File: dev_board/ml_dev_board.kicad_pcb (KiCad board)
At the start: 2 copper layers, 100 x 73.2 mm, 49 parts, among them J1 JTAG 3.3V, J2 Canon-Service-Connector, J3 USB_B_Mini, J4 Probe Connector, J5 canon_service_jumper_terminal, U1 SN74AUP1T34DCK, U2 SN74AUP1T34DCK, U3 93LCxxBxxOT, U4 LD1117S33TR_SOT223, U5 FT4232H, U6 74HC595, Y1 12MHz

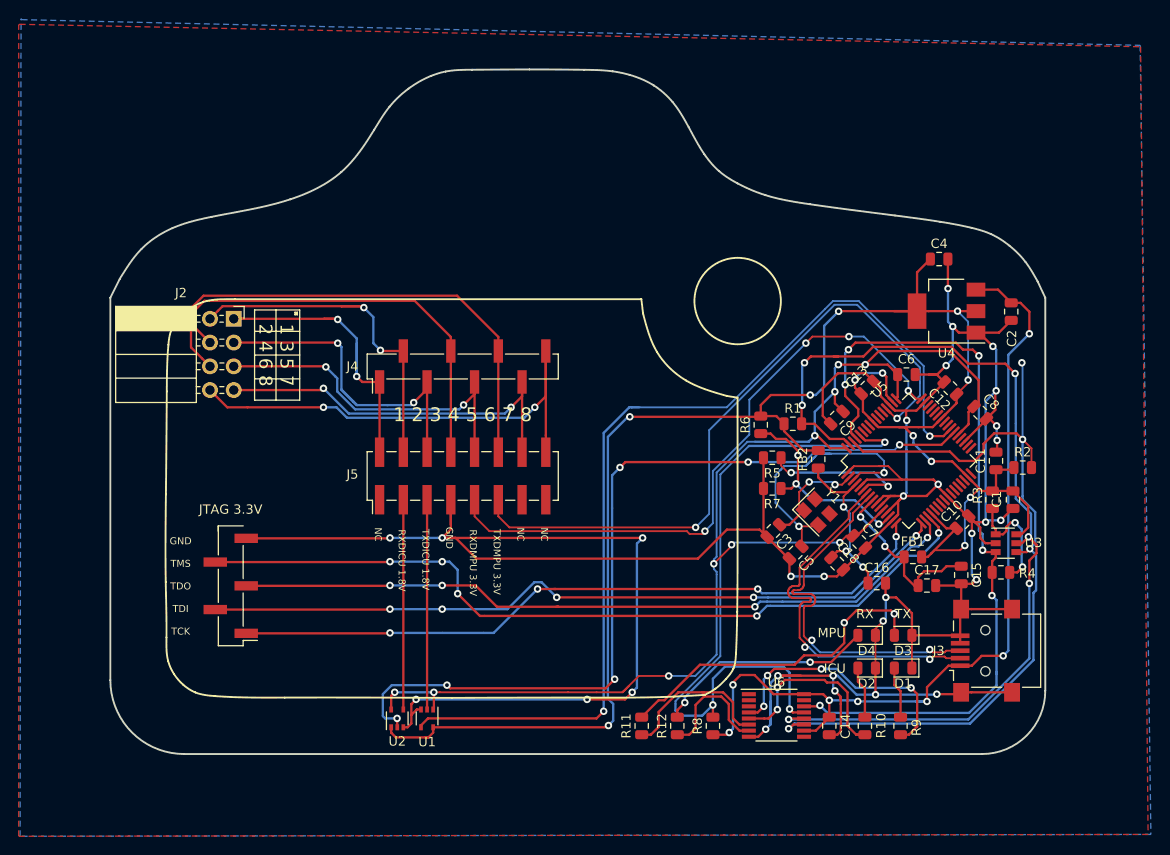
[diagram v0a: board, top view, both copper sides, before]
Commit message: dev_board: add status led + test pads
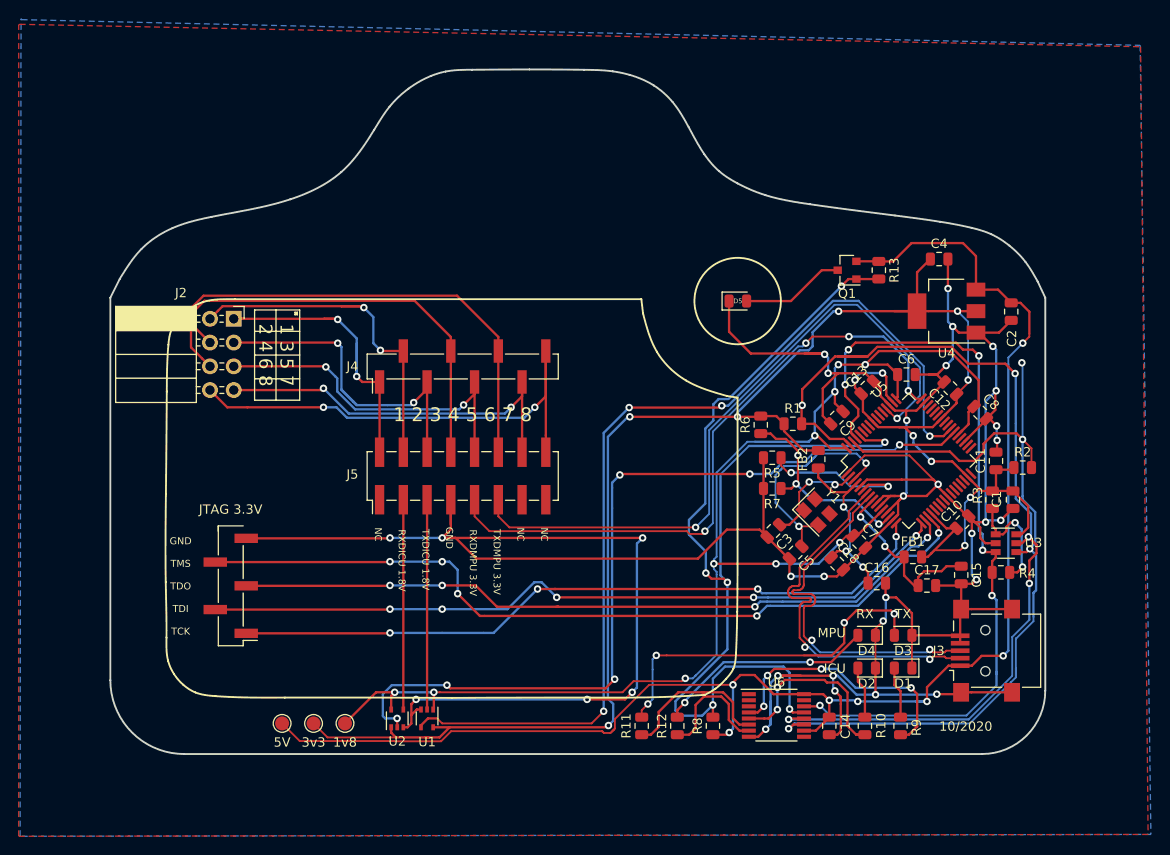
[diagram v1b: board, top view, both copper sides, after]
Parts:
- added D5: Red Status LED, LED_SMD:LED_0805_2012Metric, F.Cu at (155.3, 72.2)
- added Q1: IRLML5203, Package_TO_SOT_SMD:SOT-23, F.Cu at (167.0, 68.9)
- added R13: 4K7, Resistor_SMD:R_0805_2012Metric, F.Cu at (170.4, 68.9)
- added TP1: 5V, TestPoint:TestPoint_Pad_D1.5mm, F.Cu at (106.6, 117.4)
- added TP2: 1v8, TestPoint:TestPoint_Pad_D1.5mm, F.Cu at (113.3, 117.4)
- added TP3: 3v3, TestPoint:TestPoint_Pad_D1.5mm, F.Cu at (109.9, 117.4)
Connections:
- net Net-(R8-Pad2) renamed /FTDI/#PWREN
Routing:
- net +5V: track 92.9 -> 163.7 mm
- net /FTDI/#PWREN: track 72.7 -> 119.1 mm, vias 3 -> 6
- net GND: track 394.1 -> 417.0 mm, vias 30 -> 32
- net Net-(D5-Pad2): track 0.00 -> 11.1 mm
- net +3V3: track 201.0 -> 211.0 mm
- net +1V8: track 139.8 -> 145.6 mm
- net Net-(C5-Pad1): track 35.1 -> 29.4 mm
- net Net-(D3-Pad2): track 35.5 -> 38.4 mm, vias 2 -> 4
- net /RXDMPU: track 68.5 -> 70.0 mm
- net /FTDI/EECS: track 101.5 -> 102.7 mm, vias 6 -> 5
- net /FTDI/EECLK: track 90.2 -> 91.1 mm
- net /TXDICU: track 104.3 -> 104.0 mm, vias 2 -> 4
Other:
- board text added: "10/2020"

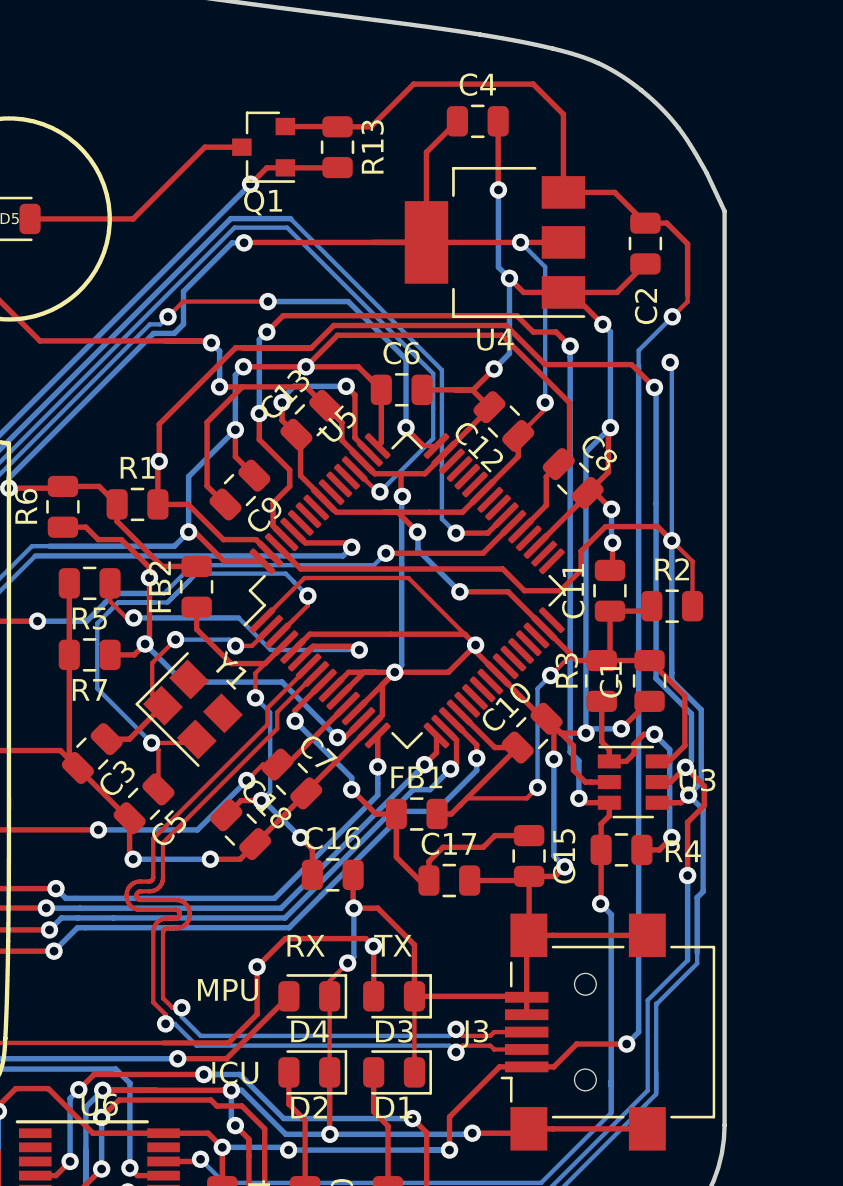
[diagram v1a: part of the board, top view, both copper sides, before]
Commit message: dev_board: add missing status LED resistor + fix silk
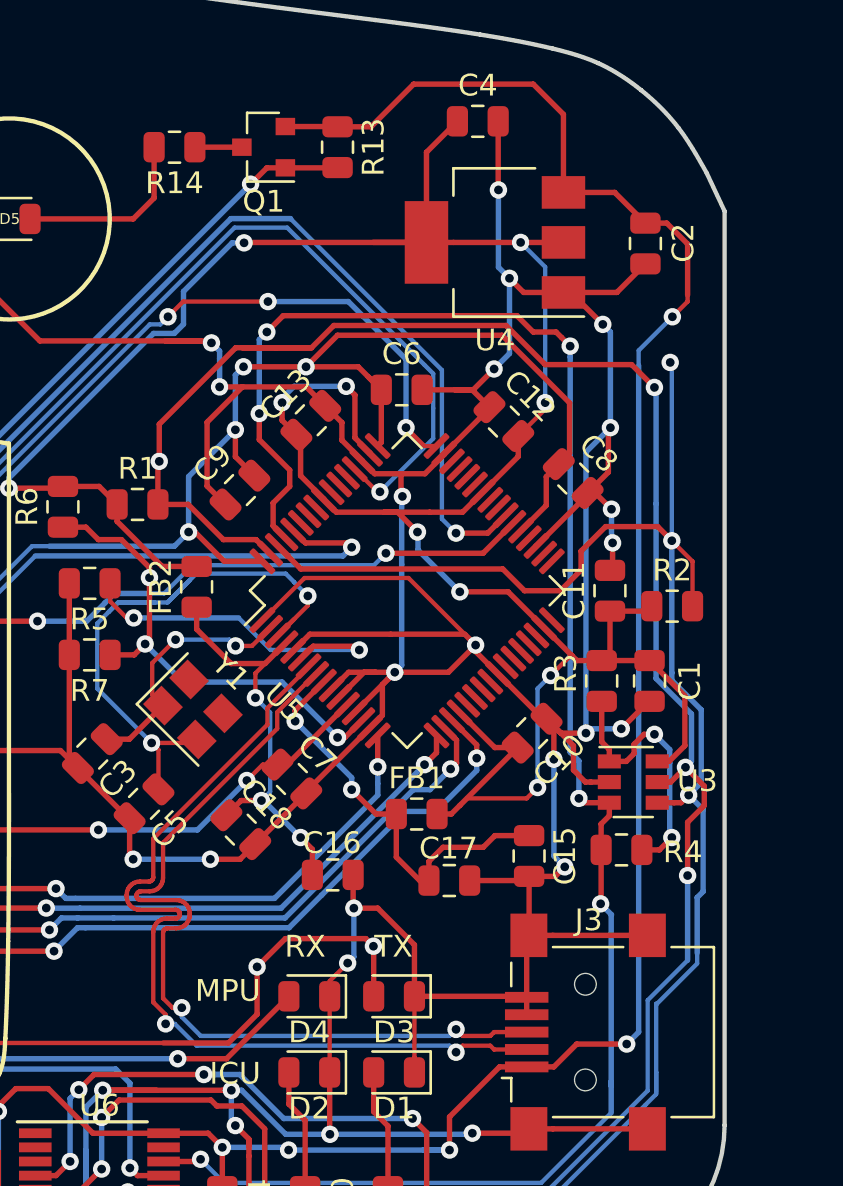
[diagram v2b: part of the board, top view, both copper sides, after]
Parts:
- added R14: 330R, Resistor_SMD:R_0805_2012Metric, F.Cu at (162.9, 68.9)
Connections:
- Q1 pad 3: Net-(D5-Pad2) -> Net-(Q1-Pad3)
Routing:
- net Net-(D5-Pad2): track 11.1 -> 8.44 mm
- net Net-(Q1-Pad3): track 0.00 -> 1.70 mm
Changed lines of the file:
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@@
     (thickness 1.6)
     (drawings 102)
-    (tracks 1282)
+    (tracks 1283)
     (zones 0)
-    (modules 55)
-    (nets 78)
+    (modules 56)
+    (nets 79)
   )
   (page A4)
@@
   )
   (setup
-    (last_trace_width 0.2)
+    (last_trace_width 0.25)
     (user_trace_width 0.2)
     (trace_clearance 0.19)
@@
     (pcbplotparams
       (layerselection 0x010fc_ffffffff)
-      (usegerberextensions false)
+      (usegerberextensions true)
       (usegerberattributes false)
       (usegerberadvancedattributes false)
@@
       (outputformat 1)
       (mirror false)
-      (drillshape 1)
+      (drillshape 0)
       (scaleselection 1)
-      (outputdirectory ""))
+      (outputdirectory "gerber/"))
   )
   (net 0 "")
@@
   (net 76 "Net-(D5-Pad2)")
   (net 77 /FTDI/#PWREN)
+  (net 78 "Net-(Q1-Pad3)")
   (net_class Default "This is the default net class."
     (clearance 0.19)
@@
     (add_net "Net-(J5-Pad17)")
     (add_net "Net-(J5-Pad18)")
+    (add_net "Net-(Q1-Pad3)")
     (add_net "Net-(R10-Pad1)")
     (add_net "Net-(R11-Pad1)")
@@
     (tags "USB USB_B USB_Mini connector")
     (attr smd)
-    (fp_text reference J3 (at 0 -5 180) (layer F.SilkS)
+    (fp_text reference J3 (at 5.15 0.15 180) (layer F.SilkS)
       (effects (font (size 1 1) (thickness 0.15)))
     )
@@
     (tags capacitor)
     (attr smd)
-    (fp_text reference C1 (at -0.07 1.74 90) (layer F.SilkS)
+    (fp_text reference C1 (at 0 -1.85 90) (layer F.SilkS)
       (effects (font (size 1 1) (thickness 0.15)))
     )
@@
     (tags capacitor)
     (attr smd)
-    (fp_text reference C2 (at 2.87 -0.07 90) (layer F.SilkS)
+    (fp_text reference C2 (at -0.03 -1.74 90) (layer F.SilkS)
       (effects (font (size 1 1) (thickness 0.15)))
     )
@@
     (tags capacitor)
     (attr smd)
-    (fp_text reference C9 (at 0 -1.65 45) (layer F.SilkS)
+    (fp_text reference C9 (at 0.028284 1.753625 45) (layer F.SilkS)
       (effects (font (size 1 1) (thickness 0.15)))
     )
@@
     (tags capacitor)
     (attr smd)
-    (fp_text reference C10 (at 0 -1.65 45) (layer F.SilkS)
+    (fp_text reference C10 (at 0 1.767767 45) (layer F.SilkS)
       (effects (font (size 1 1) (thickness 0.15)))
     )
@@
     (tags capacitor)
     (attr smd)
-    (fp_text reference C12 (at 0 -1.65 135) (layer F.SilkS)
+    (fp_text reference C12 (at -0.021213 1.675843 135) (layer F.SilkS)
       (effects (font (size 1 1) (thickness 0.15)))
     )
@@
     (tags resistor)
     (attr smd)
-    (fp_text reference R3 (at -0.47 1.57 90) (layer F.SilkS)
+    (fp_text reference R3 (at -0.35 1.65 90) (layer F.SilkS)
       (effects (font (size 1 1) (thickness 0.15)))
     )
@@
     (tags capacitor)
     (attr smd)
-    (fp_text reference C16 (at 0 -1.65) (layer F.SilkS)
+    (fp_text reference C16 (at -0.03 -1.47) (layer F.SilkS)
       (effects (font (size 1 1) (thickness 0.15)))
     )
@@
     (tags capacitor)
     (attr smd)
-    (fp_text reference C17 (at 0 -1.65) (layer F.SilkS)
+    (fp_text reference C17 (at -0.04 -1.48) (layer F.SilkS)
       (effects (font (size 1 1) (thickness 0.15)))
     )
@@
     (tags "LQFP QFP")
     (attr smd)
-    (fp_text reference U5 (at 3.181981 -7.608469 45) (layer F.SilkS)
+    (fp_text reference U5 (at -7.636753 -0.353553 135) (layer F.SilkS)
       (effects (font (size 1 1) (thickness 0.15)))
     )
@@
       (net 3 +5V))
     (pad 3 smd rect (at 1 0 180) (size 0.9 0.8) (layers F.Cu F.Paste F.Mask)
-      (net 76 "Net-(D5-Pad2)"))
+      (net 78 "Net-(Q1-Pad3)"))
     (model ${KISYS3DMOD}/Package_TO_SOT_SMD.3dshapes/SOT-23.wrl
       (at (xyz 0 0 0))
@@
       (net 1 +3V3))
   )
+  (module Resistor_SMD:R_0805_2012Metric (layer F.Cu)
+    (at 162.9 68.9 180)
+    (descr "Resistor SMD 0805 (2012 Metric), square (rectangular) end terminal, IPC_7351 nominal, (Body size source: https://docs.google.com/spreadsheets/d/1BsfQQcO9C6DZCsRaXUlFlo91Tg2WpOkGARC1WS5S8t0/edit?usp=sharing), generated with kicad-footprint-generator")
+    (tags resistor)
+    (attr smd)
+    (fp_text reference R14 (at 0 -1.65) (layer F.SilkS)
+      (effects (font (size 1 1) (thickness 0.15)))
+    )
+    (fp_text value 330R (at 0 1.65) (layer F.Fab)
+      (effects (font (size 1 1) (thickness 0.15)))
+    )
+    (fp_line (start -1 0.6) (end -1 -0.6) (layer F.Fab) (width 0.1))
+    (fp_line (start -1 -0.6) (end 1 -0.6) (layer F.Fab) (width 0.1))
+    (fp_line (start 1 -0.6) (end 1 0.6) (layer F.Fab) (width 0.1))
+    (fp_line (start 1 0.6) (end -1 0.6) (layer F.Fab) (width 0.1))
+    (fp_line (start -0.258578 -0.71) (end 0.258578 -0.71) (layer F.SilkS) (width 0.12))
+    (fp_line (start -0.258578 0.71) (end 0.258578 0.71) (layer F.SilkS) (width 0.12))
+    (fp_line (start -1.68 0.95) (end -1.68 -0.95) (layer F.CrtYd) (width 0.05))
+    (fp_line (start -1.68 -0.95) (end 1.68 -0.95) (layer F.CrtYd) (width 0.05))
+    (fp_line (start 1.68 -0.95) (end 1.68 0.95) (layer F.CrtYd) (width 0.05))
+    (fp_line (start 1.68 0.95) (end -1.68 0.95) (layer F.CrtYd) (width 0.05))
+    (fp_text user %R (at 0 0) (layer F.Fab)
+      (effects (font (size 0.5 0.5) (thickness 0.08)))
+    )
+    (pad 1 smd roundrect (at -0.9375 0 180) (size 0.975 1.4) (layers F.Cu F.Paste F.Mask) (roundrect_rratio 0.25)
+      (net 78 "Net-(Q1-Pad3)"))
+    (pad 2 smd roundrect (at 0.9375 0 180) (size 0.975 1.4) (layers F.Cu F.Paste F.Mask) (roundrect_rratio 0.25)
+      (net 76 "Net-(D5-Pad2)"))
+    (model ${KISYS3DMOD}/Resistor_SMD.3dshapes/R_0805_2012Metric.wrl
+      (at (xyz 0 0 0))
+      (scale (xyz 1 1 1))
+      (rotate (xyz 0 0 0))
+    )
+  )
   (gr_text 10/2020 (at 179.7 117.7) (layer F.SilkS)
     (effects (font (size 1 1) (thickness 0.15)))
@@
   (segment (start 169.383877 93.127215) (end 169.419231 93.127215) (width 0.2) (layer F.Cu) (net 75))
   (segment (start 161.76256 103.125) (end 161.898841 103.109644) (width 0.2) (layer F.Cu) (net 75))
-  (segment (start 166 68.9) (end 164.3 68.9) (width 0.25) (layer F.Cu) (net 76))
   (segment (start 161 72.2) (end 156.2575 72.2) (width 0.25) (layer F.Cu) (net 76))
-  (segment (start 164.3 68.9) (end 161 72.2) (width 0.25) (layer F.Cu) (net 76))
+  (segment (start 161.9625 71.2375) (end 161 72.2) (width 0.25) (layer F.Cu) (net 76))
+  (segment (start 161.9625 68.9) (end 161.9625 71.2375) (width 0.25) (layer F.Cu) (net 76))
   (via (at 152.65 115.4) (size 0.8) (drill 0.4) (layers F.Cu B.Cu) (net 77))
   (segment (start 152.654 115.404) (end 152.65 115.4) (width 0.25) (layer F.Cu) (net 77))
@@
   (segment (start 151.9 99) (end 150.088288 97.188288) (width 0.25) (layer B.Cu) (net 77))
   (segment (start 151.9 101.3) (end 151.9 99) (width 0.25) (layer B.Cu) (net 77))
+  (segment (start 166 68.9) (end 164.3 68.9) (width 0.25) (layer F.Cu) (net 78))
   (zone (net 2) (net_name GND) (layer F.Cu) (hatch edge 0.508)
     (connect_pads (clearance 0.508))
